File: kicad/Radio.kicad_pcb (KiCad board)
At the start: 2 copper layers, 129 x 89.5 mm, 35 parts, among them J1 PCB_SMA, J2 Conn_01x02, J3 PCB_SMA, J4 PCB_SMA, T1 6:31, T2 31:6, T3 T50_SPLITTER, U1 LM78L05_TO92, U2 FST3253, U3 LM358

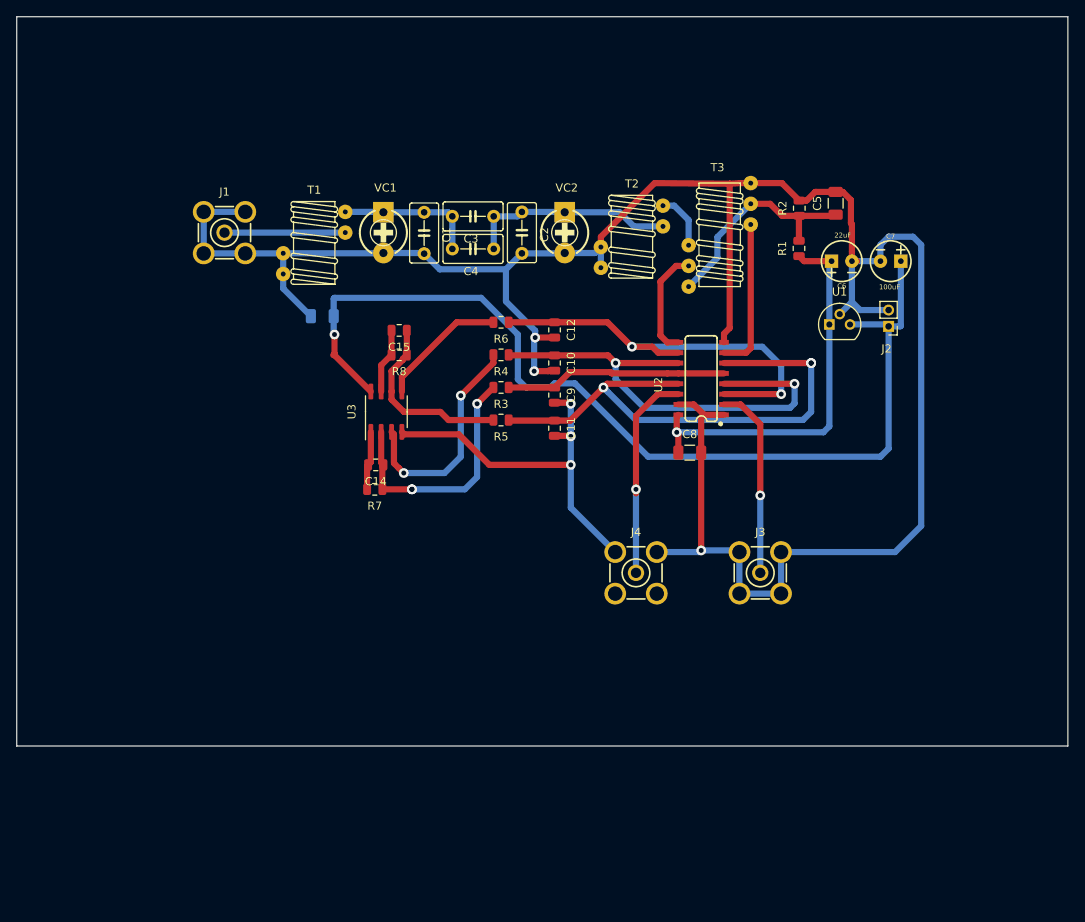
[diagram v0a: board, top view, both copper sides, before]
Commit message: Tinypico on board
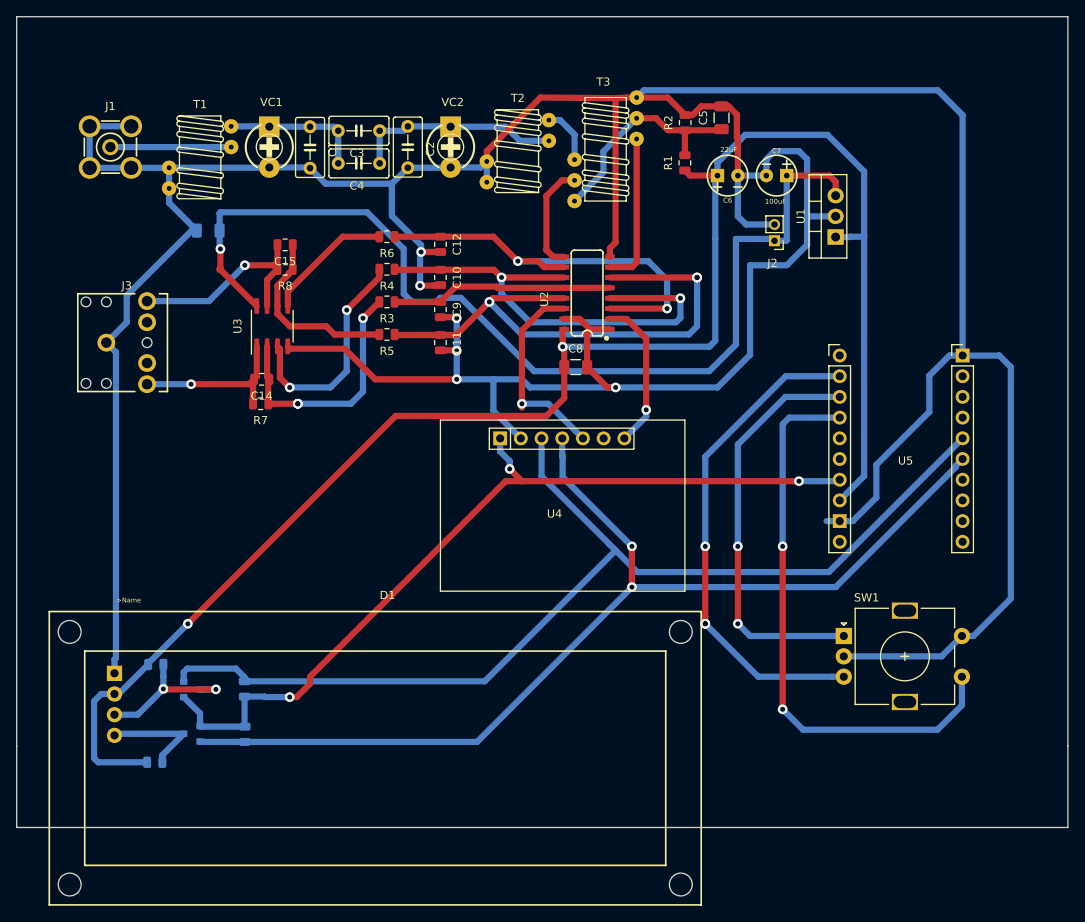
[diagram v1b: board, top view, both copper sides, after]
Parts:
- removed J4: PCB_SMA, Xenir:PCB SMA
- added D1: LCD_I2C, Xenir:LCD_I2C, F.Cu at (95.0, 103.0)
- added Q1: MOSFET-NCH-AO3404A, Package_TO_SOT_SMD:SOT-23, B.Cu at (72.0, 118.0)
- added Q2: MOSFET-NCH-AO3404A, Package_TO_SOT_SMD:SOT-23, B.Cu at (72.0, 123.5)
- added R10: 1k, Xenir:Capacitor 0805, B.Cu at (76.0, 123.6)
- added R11: 1k, Xenir:Capacitor 0805, B.Cu at (67.6, 117.5)
- added R12: 1k, Xenir:Capacitor 0805, B.Cu at (67.4, 129.5)
- added R9: 1k, Xenir:Capacitor 0805, B.Cu at (81.0, 118.0)
- added SW1: Rotary_Encoder_Switch, Rotary_Encoder:RotaryEncoder_Alps_EC11E-Switch_Vertical_H20mm, F.Cu at (152.0, 111.5)
- added U4: si5351, Xenir:si5351, F.Cu at (132.5, 85.0)
- added U5: TINYPico, Xenir:TINYpico, F.Cu at (159.6, 72.0)
- J3: value PCB_SMA -> Audio_Jack; footprint Xenir:PCB SMA -> Xenir:Audio_Jack
- U1: value LM78L05_TO92 -> LM7805_TO220; footprint Xenir:T092 -> Package_TO_SOT_THT:TO-220-3_Vertical
- moved J3 84.3 mm to (63.5, 67.0)
- moved C1 17.5 mm to (90.0, 51.0)
- moved C10 17.5 mm to (105.0, 67.5)
- moved C11 17.5 mm to (105.0, 75.5)
- moved C12 17.5 mm to (105.0, 63.4)
- moved C13 17.5 mm to (74.0, 59.0)
- moved C14 17.5 mm to (80.6, 82.5)
- moved C15 17.5 mm to (83.4, 66.0)
- moved C2 17.5 mm to (102.0, 51.0)
- moved C3 17.5 mm to (93.0, 53.0)
- moved C4 17.5 mm to (93.0, 57.0)
- moved C5 17.5 mm to (134.2, 47.9)
- moved C6 17.5 mm to (137.7, 55.0)
- moved C7 17.5 mm to (143.8, 55.0)
- moved C8 17.5 mm to (119.1, 75.8)
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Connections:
- C14 pad 2: Net-(C14-Pad2) -> I_OUTPUT
- C15 pad 2: Net-(C15-Pad2) -> Q_OUTPUT
- R7 pad 2: Net-(C14-Pad2) -> I_OUTPUT
- R8 pad 2: Net-(C15-Pad2) -> Q_OUTPUT
- U2 pad 2: Net-(J3-Pad1) -> Net-(U2-Pad2)
- U3 pad 1: Net-(C14-Pad2) -> I_OUTPUT
- U3 pad 7: Net-(C15-Pad2) -> Q_OUTPUT
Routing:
- net GND: track 327.8 -> 525.7 mm
- net +5V: track 48.7 -> 207.3 mm, vias 1 -> 2
- net SDA_LV: track 0.00 -> 128.9 mm
- net SCL_LV: track 0.00 -> 128.9 mm, vias 0 -> 2
- net +3V3: track 0.00 -> 104.6 mm, vias 0 -> 3
- net Net-(SW1-PadS1): track 0.00 -> 70.1 mm, vias 0 -> 2
- net Net-(SW1-PadB): track 0.00 -> 60.8 mm, vias 0 -> 3
- net Net-(SW1-PadA): track 0.00 -> 50.5 mm, vias 0 -> 2
- net Q_OUTPUT: track 0.00 -> 26.1 mm, vias 0 -> 1
- net Net-(J3-Pad1): track 23.7 -> 0.00 mm, vias 1 -> 0
- net I_OUTPUT: track 0.00 -> 20.6 mm, vias 0 -> 1
- net Net-(U2-Pad2): track 0.00 -> 18.8 mm, vias 0 -> 1
- net SDA_HV: track 0.00 -> 18.7 mm, vias 0 -> 2
- net SCL_HV: track 0.00 -> 13.2 mm
- net Net-(C15-Pad2): track 8.03 -> 0.00 mm
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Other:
- board size 129 x 89.5 mm -> 129 x 99.5 mm
